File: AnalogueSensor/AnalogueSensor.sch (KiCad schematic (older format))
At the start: 0 parts

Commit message: Drew up draft schematic for analogue sensor
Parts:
- added R?: R_Small, symbol Device:R_Small
- added R?: LDR03, OptoDevice:R_LDR_10x8.5mm_P7.6mm_Vertical, symbol Sensor_Optical:LDR03
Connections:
- new net GND: R?.2
- new net Vcc: R?.1
- new net Vout: R?.1, R?.2
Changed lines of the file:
@@
 Comment4 ""
 $EndDescr
+Text GLabel 2950 1850 0    50   Input ~ 0
+Vcc
+$Comp
+L Device:R_Small R?
+U 1 1 640358D9
+P 3200 2300
+F 0 "R?" H 3259 2346 50  0000 L CNN
+F 1 "R_Small" H 3259 2255 50  0000 L CNN
+F 2 "" H 3200 2300 50  0001 C CNN
+F 3 "~" H 3200 2300 50  0001 C CNN
+	1    3200 2300
+	1    0    0    -1
+$EndComp
+$Comp
+L Sensor_Optical:LDR03 R?
+U 1 1 640363B3
+P 3200 3100
+F 0 "R?" H 3270 3146 50  0000 L CNN
+F 1 "LDR03" H 3270 3055 50  0000 L CNN
+F 2 "OptoDevice:R_LDR_10x8.5mm_P7.6mm_Vertical" V 3375 3100 50  0001 C CNN
+F 3 "http://www.elektronica-componenten.nl/WebRoot/StoreNL/Shops/61422969/54F1/BA0C/C664/31B9/2173/C0A8/2AB9/2AEF/LDR03IMP.pdf" H 3200 3050 50  0001 C CNN
+	1    3200 3100
+	1    0    0    -1
+$EndComp
+Wire Wire Line
+	2950 1850 3200 1850
+Wire Wire Line
+	3200 1850 3200 2200
+Wire Wire Line
+	3200 2400 3200 2700
+$Comp
+L power:GND #PWR?
+U 1 1 64036F9E
+P 3200 3250
+F 0 "#PWR?" H 3200 3000 50  0001 C CNN
+F 1 "GND" H 3205 3077 50  0000 C CNN
+F 2 "" H 3200 3250 50  0001 C CNN
+F 3 "" H 3200 3250 50  0001 C CNN
+	1    3200 3250
+	1    0    0    -1
+$EndComp
+Text GLabel 4050 2700 2    50   Input ~ 0
+Vout
+Wire Wire Line
+	3200 2700 4050 2700
+Connection ~ 3200 2700
+Wire Wire Line
+	3200 2700 3200 2950
 $EndSCHEMATC

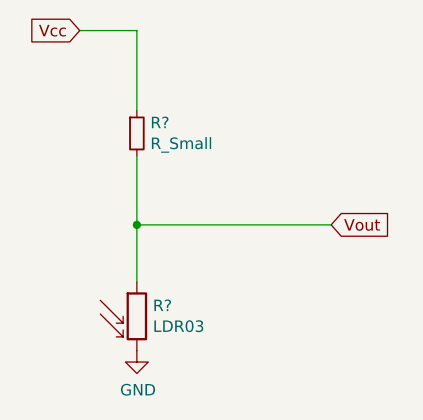
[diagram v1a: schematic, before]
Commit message: added component values
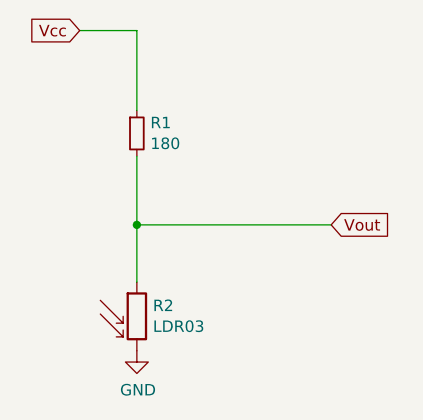
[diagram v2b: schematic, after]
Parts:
- R1: renamed from R?; value R_Small -> 180; footprint (none) -> Resistor_SMD:R_0201_0603Metric; Populate (none) -> yes
- R2: renamed from R?; Populate (none) -> yes
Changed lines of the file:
@@
 Vcc
 $Comp
-L Device:R_Small R?
+L Device:R_Small R1
 U 1 1 640358D9
 P 3200 2300
-F 0 "R?" H 3259 2346 50  0000 L CNN
-F 1 "R_Small" H 3259 2255 50  0000 L CNN
-F 2 "" H 3200 2300 50  0001 C CNN
+F 0 "R1" H 3259 2346 50  0000 L CNN
+F 1 "180" H 3259 2255 50  0000 L CNN
+F 2 "Resistor_SMD:R_0201_0603Metric" H 3200 2300 50  0001 C CNN
 F 3 "~" H 3200 2300 50  0001 C CNN
+F 4 "yes" H 3200 2300 50  0001 C CNN "Populate"
 	1    3200 2300
 	1    0    0    -1
 $EndComp
 $Comp
-L Sensor_Optical:LDR03 R?
+L Sensor_Optical:LDR03 R2
 U 1 1 640363B3
 P 3200 3100
-F 0 "R?" H 3270 3146 50  0000 L CNN
+F 0 "R2" H 3270 3146 50  0000 L CNN
 F 1 "LDR03" H 3270 3055 50  0000 L CNN
 F 2 "OptoDevice:R_LDR_10x8.5mm_P7.6mm_Vertical" V 3375 3100 50  0001 C CNN
 F 3 "http://www.elektronica-componenten.nl/WebRoot/StoreNL/Shops/61422969/54F1/BA0C/C664/31B9/2173/C0A8/2AB9/2AEF/LDR03IMP.pdf" H 3200 3050 50  0001 C CNN
+F 4 "yes" H 3200 3100 50  0001 C CNN "Populate"
 	1    3200 3100
 	1    0    0    -1
@@
 	3200 2400 3200 2700
 $Comp
-L power:GND #PWR?
+L power:GND #PWR0101
 U 1 1 64036F9E
 P 3200 3250
-F 0 "#PWR?" H 3200 3000 50  0001 C CNN
+F 0 "#PWR0101" H 3200 3000 50  0001 C CNN
 F 1 "GND" H 3205 3077 50  0000 C CNN
 F 2 "" H 3200 3250 50  0001 C CNN

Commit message: finalising draft schematics
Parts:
- R1: Price (none) -> 0.0017
- R2: Price (none) -> 0.04
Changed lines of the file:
@@
 F 3 "~" H 3200 2300 50  0001 C CNN
 F 4 "yes" H 3200 2300 50  0001 C CNN "Populate"
+F 5 "0.0017" H 3200 2300 50  0001 C CNN "Price"
 	1    3200 2300
 	1    0    0    -1
@@
 F 3 "http://www.elektronica-componenten.nl/WebRoot/StoreNL/Shops/61422969/54F1/BA0C/C664/31B9/2173/C0A8/2AB9/2AEF/LDR03IMP.pdf" H 3200 3050 50  0001 C CNN
 F 4 "yes" H 3200 3100 50  0001 C CNN "Populate"
+F 5 "0.04" H 3200 3100 50  0001 C CNN "Price"
 	1    3200 3100
 	1    0    0    -1
